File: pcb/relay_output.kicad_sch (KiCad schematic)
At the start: 9 parts, among them J23 Screw_Terminal_01x03, K6 Relay_SPDT, Q13 NDS355AN

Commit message: Use larger screw terminals, adjust layout to suit
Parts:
- J23: footprint Conn_ScrewTerminals:ED5553DS -> Conn_ScrewTerminals:CTB7000-3
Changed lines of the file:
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@@
 	(label "NO"
 		(at 189.23 86.36 0)
-		(fields_autoplaced yes)
 		(effects
 			(font
@@
 	(label "COM"
 		(at 194.31 88.9 0)
-		(fields_autoplaced yes)
 		(effects
 			(font
@@
 	(label "NC"
 		(at 184.15 86.36 180)
-		(fields_autoplaced yes)
 		(effects
 			(font
@@
 		(shape input)
 		(at 82.55 114.3 180)
-		(fields_autoplaced yes)
 		(effects
 			(font
@@
 			)
 		)
-		(property "Footprint" "Conn_ScrewTerminals:ED5553DS"
+		(property "Footprint" "Conn_ScrewTerminals:CTB7000-3"
 			(at 186.69 80.01 0)
 			(effects

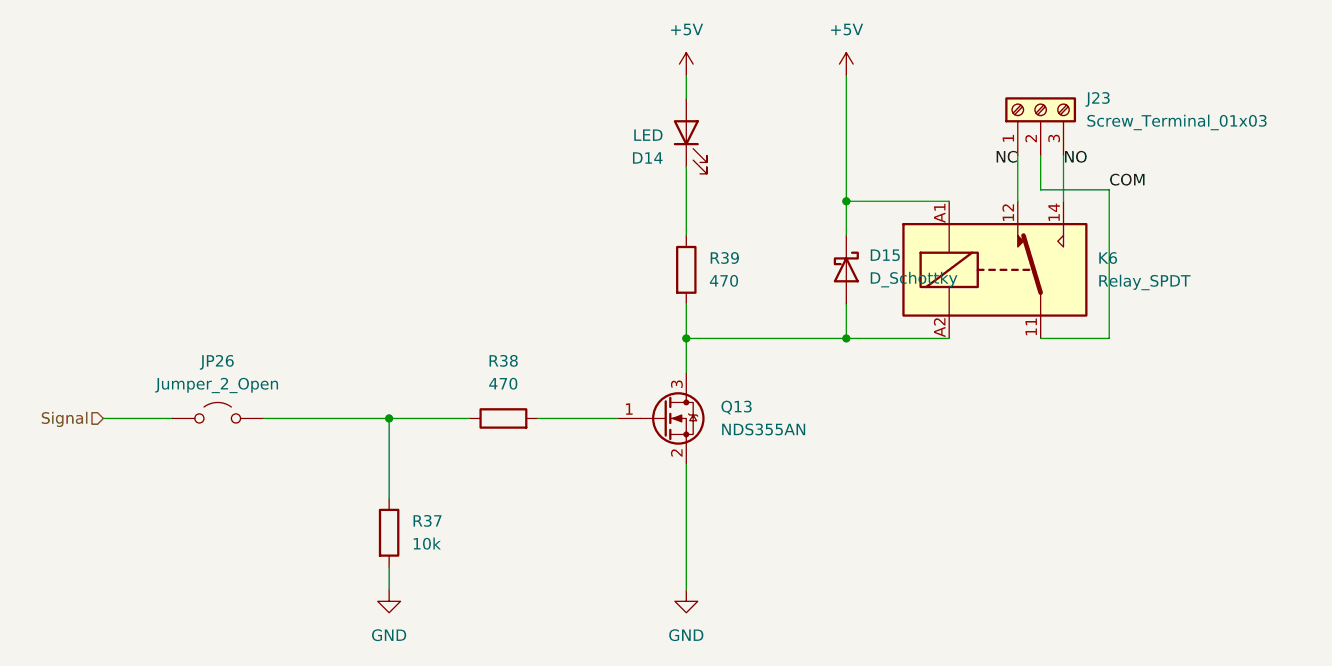
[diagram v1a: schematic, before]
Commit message: Convert PCB to KiCad 9 project
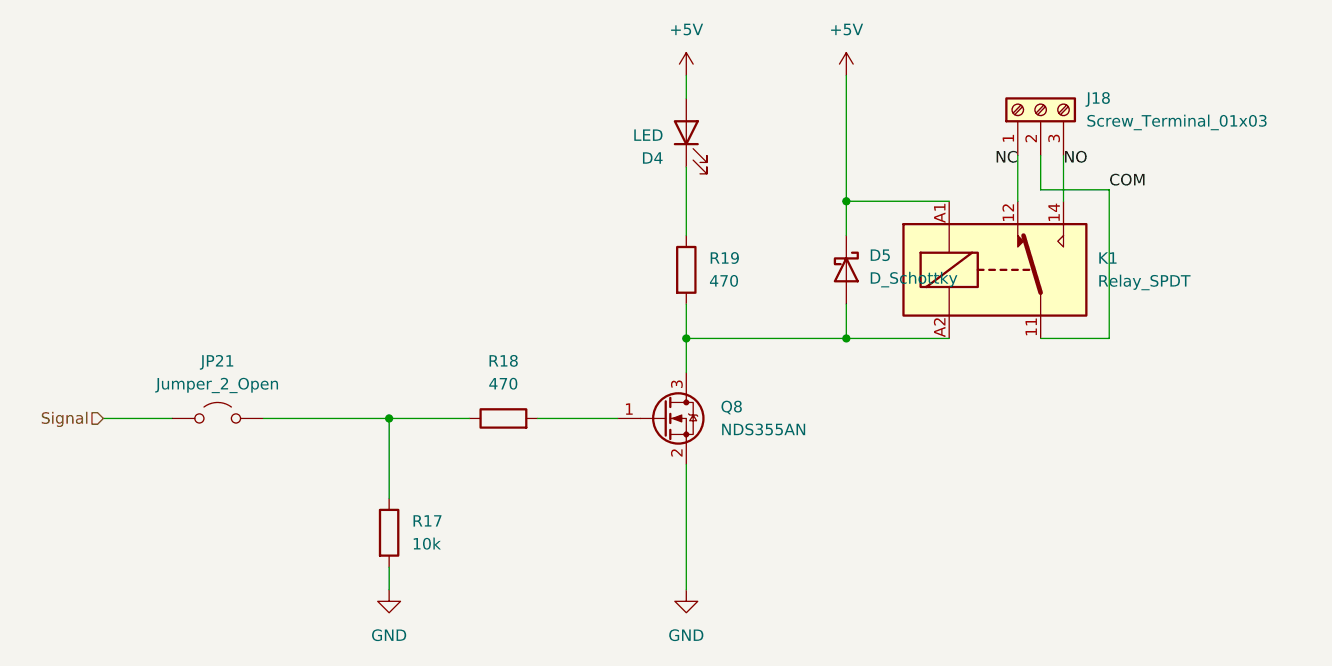
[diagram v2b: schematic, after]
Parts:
- renumbered D14 to D4, D15 to D5, J23 to J18, JP26 to JP21, K6 to K1, Q13 to Q8, R37 to R17, R38 to R18, R39 to R19
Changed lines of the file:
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@@
 (kicad_sch
-	(version 20231120)
+	(version 20250114)
 	(generator "eeschema")
-	(generator_version "8.0")
+	(generator_version "9.0")
 	(paper "A4")
 	(junction
@@
 		(dnp no)
 		(fields_autoplaced yes)
-		(property "Reference" "R38"
+		(property "Reference" "R18"
 			(at 127 107.95 90)
 			(effects
@@
 		(dnp no)
 		(fields_autoplaced yes)
-		(property "Reference" "JP26"
+		(property "Reference" "JP21"
 			(at 95.25 107.95 0)
 			(effects
@@
 		(dnp no)
 		(fields_autoplaced yes)
-		(property "Reference" "#PWR090"
+		(property "Reference" "#PWR070"
 			(at 147.32 139.7 0)
 			(effects
@@
 		(dnp no)
 		(fields_autoplaced yes)
-		(property "Reference" "#PWR089"
+		(property "Reference" "#PWR069"
 			(at 147.32 80.01 0)
 			(effects
@@
 		(dnp no)
 		(fields_autoplaced yes)
-		(property "Reference" "K6"
+		(property "Reference" "K1"
 			(at 193.04 96.5199 0)
 			(effects
@@
 		(dnp no)
 		(fields_autoplaced yes)
-		(property "Reference" "#PWR088"
+		(property "Reference" "#PWR068"
 			(at 114.3 139.7 0)
 			(effects
@@
 		(dnp no)
 		(fields_autoplaced yes)
-		(property "Reference" "D15"
+		(property "Reference" "D5"
 			(at 167.64 96.2024 90)
 			(effects
@@
 		(dnp no)
 		(fields_autoplaced yes)
-		(property "Reference" "#PWR091"
+		(property "Reference" "#PWR071"
 			(at 165.1 80.01 0)
 			(effects
@@
 		(dnp no)
 		(fields_autoplaced yes)
-		(property "Reference" "R39"
+		(property "Reference" "R19"
 			(at 149.86 96.5199 0)
 			(effects
@@
 		(dnp no)
 		(fields_autoplaced yes)
-		(property "Reference" "J23"
+		(property "Reference" "J18"
 			(at 191.77 78.7399 90)
 			(effects
@@
 		(on_board yes)
 		(dnp no)
-		(property "Reference" "D14"
+		(property "Reference" "D4"
 			(at 144.78 85.4076 90)
 			(effects
@@
 		(dnp no)
 		(fields_autoplaced yes)
-		(property "Reference" "Q13"
+		(property "Reference" "Q8"
 			(at 151.13 113.0299 0)
 			(effects
@@
 		(dnp no)
 		(fields_autoplaced yes)
-		(property "Reference" "R37"
+		(property "Reference" "R17"
 			(at 116.84 125.7299 0)
 			(effects
